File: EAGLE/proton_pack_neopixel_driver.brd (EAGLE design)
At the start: 35.3 x 15.4 mm, 7 parts

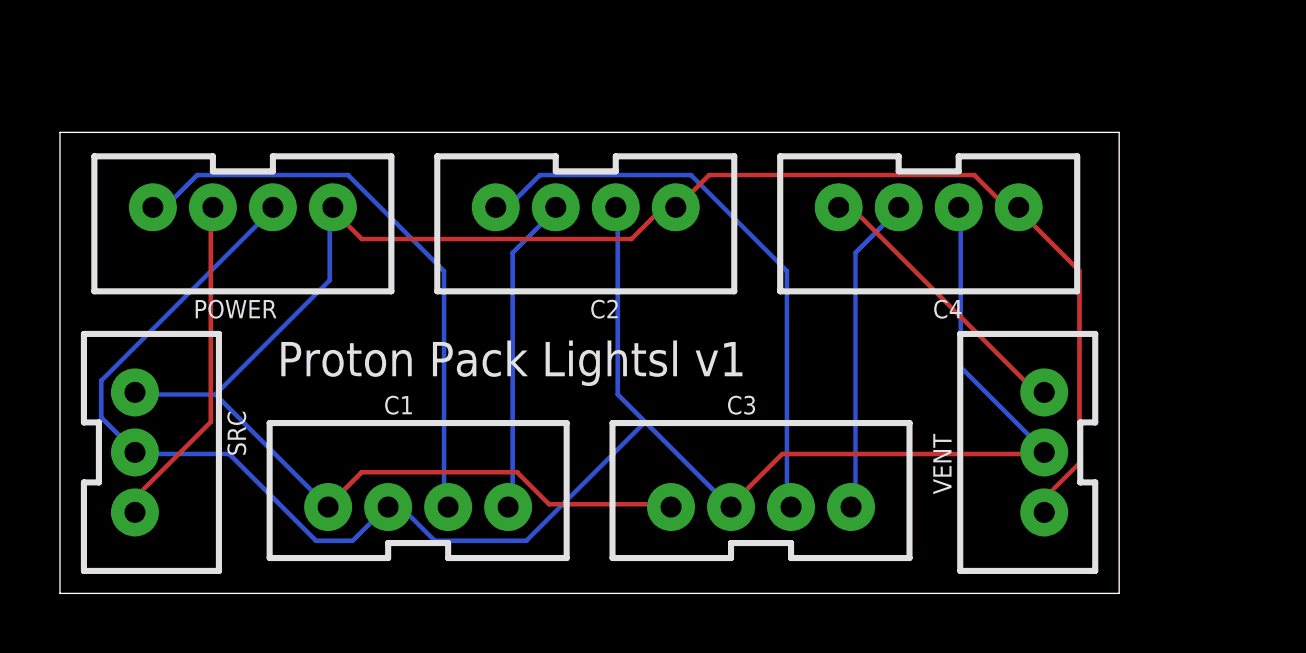
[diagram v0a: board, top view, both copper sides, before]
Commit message: update the light board to use the same jst lib as the other one.
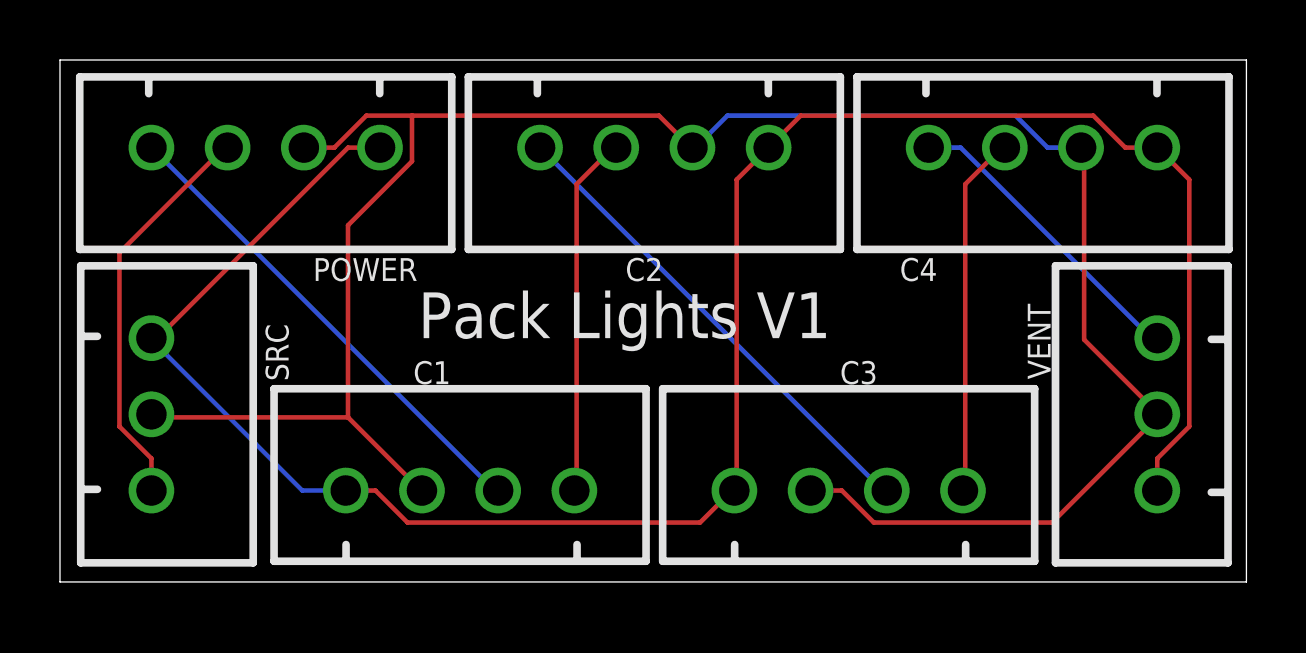
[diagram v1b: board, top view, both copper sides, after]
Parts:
- C1, C2, C3, C4, POWER: value (none) -> JST-XH-04-PIN-ROUND-PAD; device SparkFun-Connectors:JST-4-PTH-VERT -> Rembrandt Electronics - JST XH Connectors v1-0:JST-XH-04-PACKAGE-ROUND-PAD
- SRC, VENT: value (none) -> JST-XH-03-PIN-ROUND-PAD; device SparkFun-Connectors:JST-3-PTH-VERT -> Rembrandt Electronics - JST XH Connectors v1-0:JST-XH-03-PACKAGE-ROUND-PAD
- moved C4 4.58 mm to (33.5, 15.2)
- moved VENT 4.50 mm to (37.3, 6.35)
- moved C2 3.42 mm to (20.6, 15.2)
- moved C3 2.92 mm to (27.1, 3.81)
- moved POWER 2.65 mm to (7.62, 15.2)
- moved C1 1.40 mm to (14.1, 3.81)
- moved SRC 1.27 mm to (3.81, 6.35)
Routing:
- net N$6: track 63.9 -> 72.3 mm
- net N$8: track 64.4 -> 70.9 mm
- net N$1: track 19.4 -> 16.3 mm
- net N$3: track 19.4 -> 16.3 mm
- net N$9: track 11.2 -> 13.4 mm
- net N$4: track 10.7 -> 12.1 mm
- net N$2: track 10.7 -> 12.1 mm
- net N$5: track 9.44 -> 10.3 mm
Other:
- board size 35.3 x 15.4 mm -> 39.5 x 17.4 mm
- board text added: "Pack Lights V1"
- board text removed: "Proton Pack Lightsl v1"
